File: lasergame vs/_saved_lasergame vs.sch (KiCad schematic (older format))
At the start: 11 parts, among them J1 USB_B, J2 Screw_Terminal_01x02, SW1 SW_SPST, SW2 SW_Reed, U1 ATmega328-PU, Y1 Crystal

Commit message: updated the schematics
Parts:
- added BZ1: Buzzer, symbol Device:Buzzer
- added D1: LED, symbol Device:LED
- added J3: Conn_01x04_Female, symbol Connector:Conn_01x04_Female
- added J4, J5, J6, J8: Screw_Terminal_01x02, symbol Connector:Screw_Terminal_01x02
- added J7: Conn_01x06_Female, symbol Connector:Conn_01x06_Female
- added Q1: IRLB8721PBF, Package_TO_SOT_THT:TO-220-3_Vertical, symbol Transistor_FET:IRLB8721PBF
- added R3, R4: R, symbol Device:R
- added SW3, SW4: SW_SPST, symbol Switch:SW_SPST
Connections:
- net +5V: now also J3.3 (Pin_3), J6.1 (Pin_1), J7.3 (Pin_3)
- net Buzzer: now also BZ1.1 (-)
- net Clock: now also J3.1 (Pin_1)
- net DIO: now also J3.2 (Pin_2)
- net DTR: now also J7.6 (Pin_6)
- net GND: now also SW2.2, BZ1.2 (+), D1.1 (K), J3.4 (Pin_4), J4.2 (Pin_2), J5.2 (Pin_2), J7.1 (Pin_1), J8.2 (Pin_2), Q1.3 (S), SW3.2 (B), SW4.2 (B)
- net LED: now also J8.1 (Pin_1), R4.2
- net Light: now also R3.1
- net Reload: now also J5.1 (Pin_1)
- net ResetButton: now also SW2.1
- net Scroll: now also SW4.1 (A)
- net SelectButton: now also SW3.1 (A)
- net Trigger: now also J4.1 (Pin_1)
- net RX: now reaches U1.2 (PD0)
- net RX: now also J7.4 (Pin_4)
- net TX: now reaches U1.3 (PD1)
- net TX: now also J7.5 (Pin_5)
- new net: Q1.1 (G), R3.2
- new net: J6.2 (Pin_2), Q1.2 (D)
- new net: D1.2 (A), R4.1
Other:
- note added: "Reload and trigger"
- note added: "Shooting LED"
- note added: "USB power input"
- note added: "buzzer"
- note added: "display"
- note added: "programming port"
- note added: "scroll and selectbutton"
- note added: "spelreset"
- note added: "uc reset"
- moved on the sheet: C3, R2, SW1, SW2

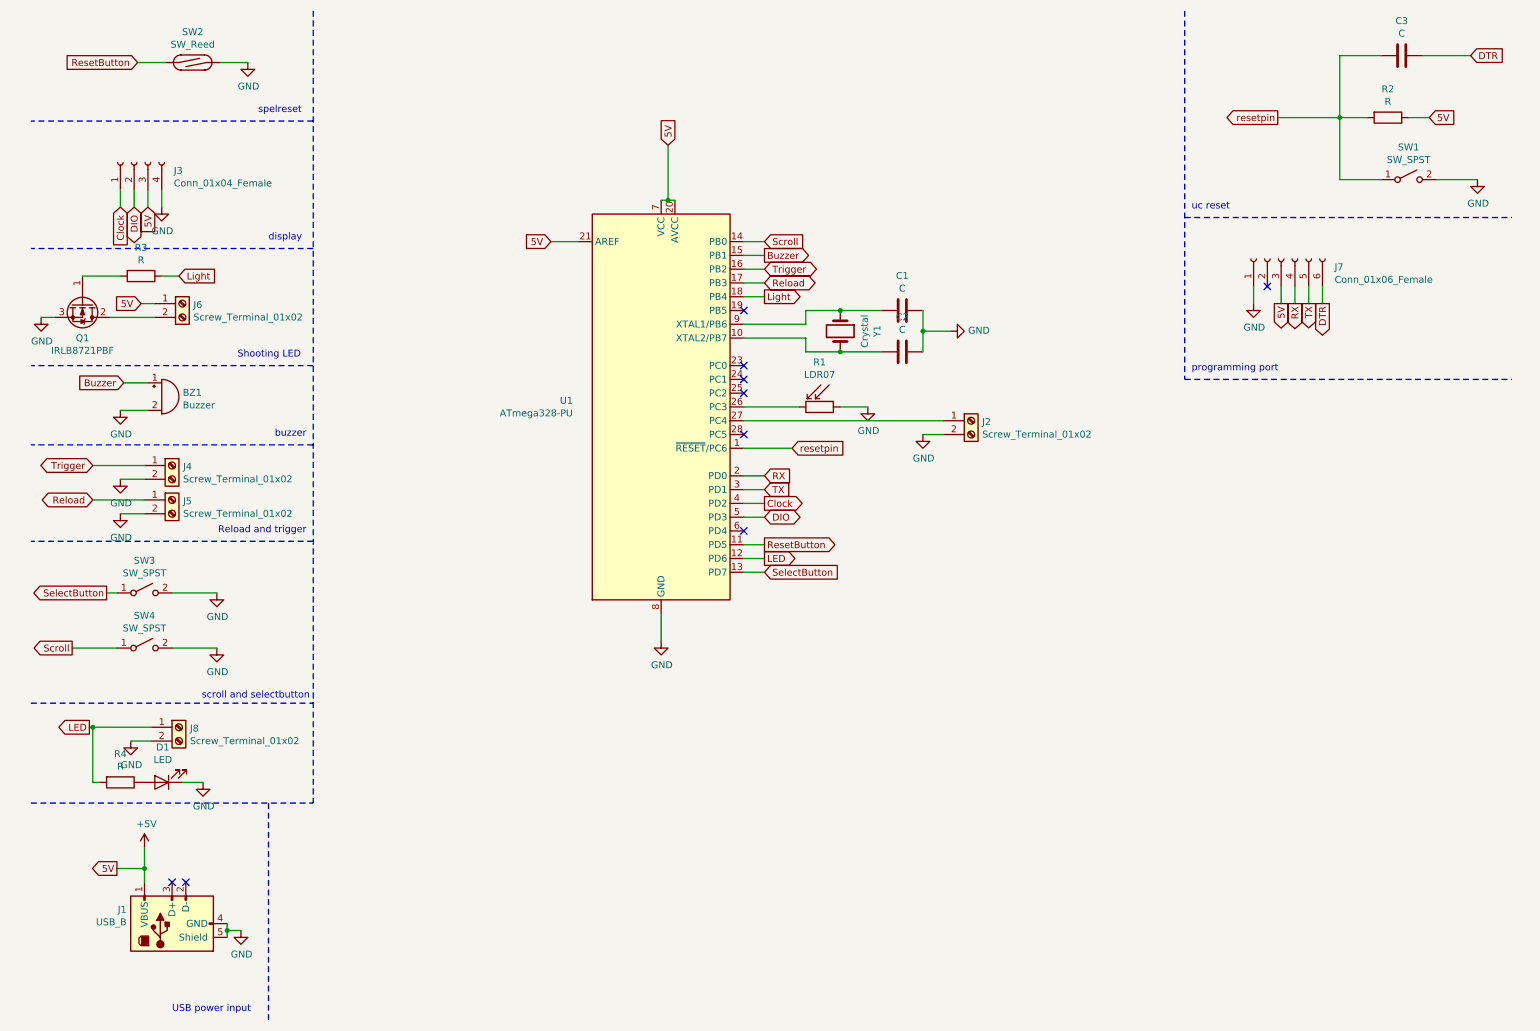
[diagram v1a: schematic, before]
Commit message: updated schematics, 2nd PCB for LDR's and LED's
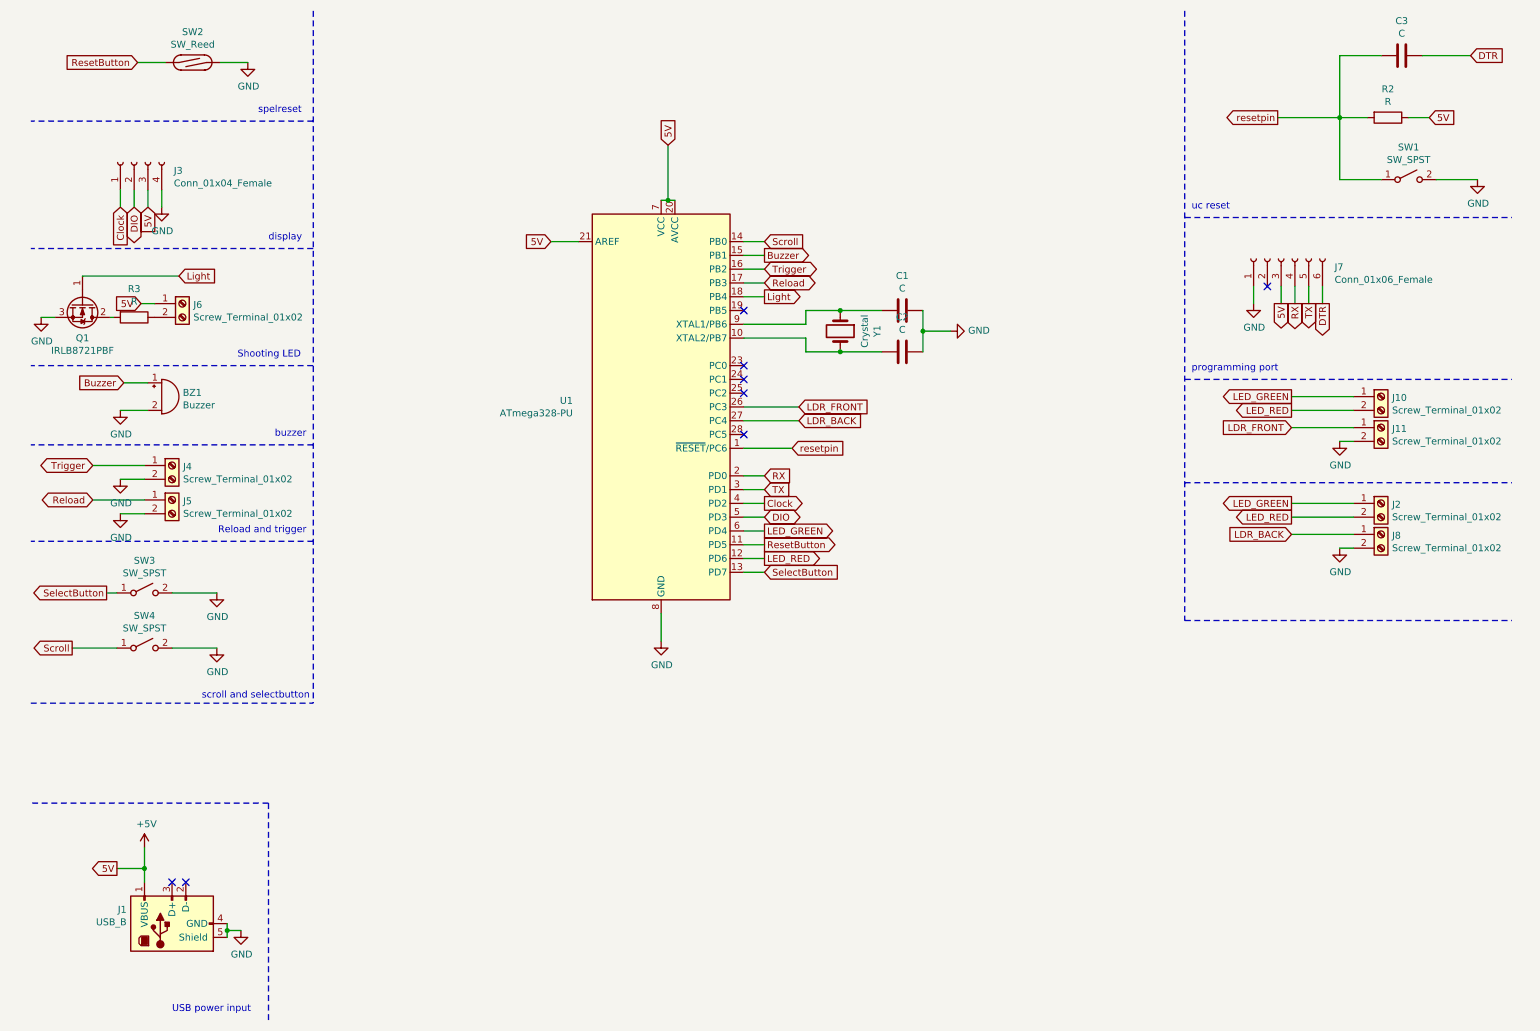
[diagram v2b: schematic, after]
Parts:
- removed D1: LED, symbol Device:LED
- removed R1: LDR07, OptoDevice:R_LDR_5.1x4.3mm_P3.4mm_Vertical, symbol Sensor_Optical:LDR07
- removed R4: R, symbol Device:R
- added J10, J11: Screw_Terminal_01x02, TerminalBlocks_Phoenix:TerminalBlock_Phoenix_MKDS1.5-2pol, symbol Connector:Screw_Terminal_01x02
- BZ1: footprint (none) -> Buzzers_Beepers:BUZZER
- C1, C2: footprint (none) -> Capacitors_THT:C_Disc_D3.4mm_W2.1mm_P2.50mm
- C3: footprint (none) -> Capacitors_SMD:C_1206_HandSoldering
- J1: footprint (none) -> Connectors:USB_B
- J2, J4, J5, J6, J8: footprint (none) -> TerminalBlocks_Phoenix:TerminalBlock_Phoenix_MKDS1.5-2pol
- J3: footprint (none) -> Pin_Headers:Pin_Header_Straight_1x04_Pitch2.54mm
- J7: footprint (none) -> Pin_Headers:Pin_Header_Straight_1x06_Pitch2.54mm
- Q1: footprint Package_TO_SOT_THT:TO-220-3_Vertical -> TO_SOT_Packages_THT:TO-220-3_Vertical
- R2: footprint (none) -> Resistors_THT:R_Axial_DIN0309_L9.0mm_D3.2mm_P12.70mm_Horizontal
- R3: footprint (none) -> Resistors_THT:R_Axial_DIN0516_L15.5mm_D5.0mm_P20.32mm_Horizontal
- SW1, SW3, SW4: footprint (none) -> Buttons_Switches_THT:SW_PUSH_6mm_h9.5mm
- SW2: footprint (none) -> reed switch:Reed Switch THT
- U1: footprint Package_DIP:DIP-28_W7.62mm -> Housings_DIP:DIP-28_W7.62mm
- Y1: footprint (none) -> Crystals:Crystal_HC49-U_Vertical
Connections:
- net GND: now also J11.2 (Pin_2); no longer J2.2 (Pin_2)
- net Light: now also Q1.1 (G); no longer R3.1
- net LDR_FRONT: now reaches U1.26 (PC3)
- net LDR_FRONT: now also J11.1 (Pin_1)
- net LDR_BACK: now reaches U1.27 (PC4)
- net LDR_BACK: now also J8.1 (Pin_1); no longer J2.1 (Pin_1)
- net LED_GREEN: now reaches U1.6 (PD4)
- net LED_GREEN: now also J2.1 (Pin_1), J10.1 (Pin_1)
- net at R3.2: now also Q1.2 (D); no longer Q1.1 (G)
- net at J6.2 (Pin_2): now also R3.1; no longer Q1.2 (D)
- net LED renamed LED_RED
- net LED_RED: now also J2.2 (Pin_2), J10.2 (Pin_2); no longer J8.1 (Pin_1)
- no-connect marks 9 -> 8
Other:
- moved on the sheet: R3

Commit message: first prototype pcb ordered
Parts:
- removed J1: USB_B, Connectors:USB_B, symbol Connector:USB_B
- added J1: 9v input, TerminalBlock_Phoenix:TerminalBlock_Phoenix_MKDS-1,5-2-5.08_1x02_P5.08mm_Horizontal, symbol Connector:Screw_Terminal_01x02
- added R1, R4: 100 ohm, Resistor_THT:R_Axial_DIN0309_L9.0mm_D3.2mm_P12.70mm_Horizontal, symbol Device:R
- added R5, R6: R, Resistor_THT:R_Axial_DIN0309_L9.0mm_D3.2mm_P12.70mm_Horizontal, symbol Device:R
- added R7: 1 Mohm, Resistor_THT:R_Axial_DIN0309_L9.0mm_D3.2mm_P12.70mm_Horizontal, symbol Device:R
- added R8: 10 kohm, Resistor_THT:R_Axial_DIN0309_L9.0mm_D3.2mm_P12.70mm_Horizontal, symbol Device:R
- added U2: L7805, Package_TO_SOT_THT:TO-220-3_Vertical, symbol Regulator_Linear:L7805
- BZ1: footprint Buzzers_Beepers:BUZZER -> Buzzer_Beeper:Buzzer_12x9.5RM7.6
- C1, C2: footprint Capacitors_THT:C_Disc_D3.4mm_W2.1mm_P2.50mm -> Capacitor_THT:C_Disc_D5.0mm_W2.5mm_P2.50mm
- C3: value C -> C_reset; footprint Capacitors_SMD:C_1206_HandSoldering -> Capacitor_THT:C_Disc_D5.0mm_W2.5mm_P2.50mm
- J10: value Screw_Terminal_01x02 -> LED Front; footprint TerminalBlocks_Phoenix:TerminalBlock_Phoenix_MKDS1.5-2pol -> TerminalBlock_Phoenix:TerminalBlock_Phoenix_MKDS-1,5-2-5.08_1x02_P5.08mm_Horizontal
- J11: value Screw_Terminal_01x02 -> LDR Front; footprint TerminalBlocks_Phoenix:TerminalBlock_Phoenix_MKDS1.5-2pol -> TerminalBlock_Phoenix:TerminalBlock_Phoenix_MKDS-1,5-2-5.08_1x02_P5.08mm_Horizontal
- J2: value Screw_Terminal_01x02 -> LED Back; footprint TerminalBlocks_Phoenix:TerminalBlock_Phoenix_MKDS1.5-2pol -> TerminalBlock_Phoenix:TerminalBlock_Phoenix_MKDS-1,5-2-5.08_1x02_P5.08mm_Horizontal
- J3: value Conn_01x04_Female -> 7 segment display; footprint Pin_Headers:Pin_Header_Straight_1x04_Pitch2.54mm -> Connector_PinHeader_2.54mm:PinHeader_1x04_P2.54mm_Vertical
- J4: value Screw_Terminal_01x02 -> Trigger; footprint TerminalBlocks_Phoenix:TerminalBlock_Phoenix_MKDS1.5-2pol -> TerminalBlock_Phoenix:TerminalBlock_Phoenix_MKDS-1,5-2-5.08_1x02_P5.08mm_Horizontal
- J5: value Screw_Terminal_01x02 -> Reload; footprint TerminalBlocks_Phoenix:TerminalBlock_Phoenix_MKDS1.5-2pol -> TerminalBlock_Phoenix:TerminalBlock_Phoenix_MKDS-1,5-2-5.08_1x02_P5.08mm_Horizontal
- J6: value Screw_Terminal_01x02 -> Fire_light; footprint TerminalBlocks_Phoenix:TerminalBlock_Phoenix_MKDS1.5-2pol -> TerminalBlock_Phoenix:TerminalBlock_Phoenix_MKDS-1,5-2-5.08_1x02_P5.08mm_Horizontal
- J7: value Conn_01x06_Female -> Programming pins; footprint Pin_Headers:Pin_Header_Straight_1x06_Pitch2.54mm -> Connector_PinHeader_2.54mm:PinHeader_1x06_P2.54mm_Vertical
- J8: value Screw_Terminal_01x02 -> LDR Back; footprint TerminalBlocks_Phoenix:TerminalBlock_Phoenix_MKDS1.5-2pol -> TerminalBlock_Phoenix:TerminalBlock_Phoenix_MKDS-1,5-2-5.08_1x02_P5.08mm_Horizontal
- Q1: footprint TO_SOT_Packages_THT:TO-220-3_Vertical -> Package_TO_SOT_THT:TO-220-3_Vertical
- R2: value R -> R_Reset; footprint Resistors_THT:R_Axial_DIN0309_L9.0mm_D3.2mm_P12.70mm_Horizontal -> Resistor_THT:R_Axial_DIN0309_L9.0mm_D3.2mm_P12.70mm_Horizontal
- R3: footprint Resistors_THT:R_Axial_DIN0516_L15.5mm_D5.0mm_P20.32mm_Horizontal -> Resistor_THT:R_Axial_DIN0516_L15.5mm_D5.0mm_P20.32mm_Horizontal
- SW1: value SW_SPST -> SW_RESET; footprint Buttons_Switches_THT:SW_PUSH_6mm_h9.5mm -> Button_Switch_THT:SW_PUSH_6mm_H9.5mm
- SW3: value SW_SPST -> Select_button; footprint Buttons_Switches_THT:SW_PUSH_6mm_h9.5mm -> Button_Switch_THT:SW_PUSH_6mm_H9.5mm
- SW4: value SW_SPST -> Scroll_button; footprint Buttons_Switches_THT:SW_PUSH_6mm_h9.5mm -> Button_Switch_THT:SW_PUSH_6mm_H9.5mm
- U1: footprint Housings_DIP:DIP-28_W7.62mm -> Package_DIP:DIP-28_W7.62mm_Socket
- Y1: footprint Crystals:Crystal_HC49-U_Vertical -> Crystal:Crystal_HC49-U_Vertical
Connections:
- net GND: now also J1.1 (Pin_1), R7.2, U2.2 (GND)
- net LDR_BACK: now also R5.2
- net LDR_FRONT: now also R6.2
- net LED_GREEN: now also R1.1; no longer U1.6 (PD4)
- net LED_RED: now also R4.1; no longer U1.12 (PD6)
- net Light: now also R7.1, R8.1; no longer U1.18 (PB4)
- net +5V renamed 5V
- net 5V: now also R5.1, R6.1, U2.3 (OUT)
- new net: R4.2, U1.12 (PD6)
- new net: R8.2, U1.18 (PB4)
- new net: R1.2, U1.6 (PD4)
- new net +9V: J1.2 (Pin_2), U2.1 (IN)
- no-connect marks 8 -> 6
